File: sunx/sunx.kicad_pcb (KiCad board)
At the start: 2 copper layers, 54 x 32 mm, 11 parts, among them J1 Conn_01x05_Socket, J2 Conn_01x04_Socket, U1 HT7333-3-SOT89, con1 Conn_01x08_MountingPin

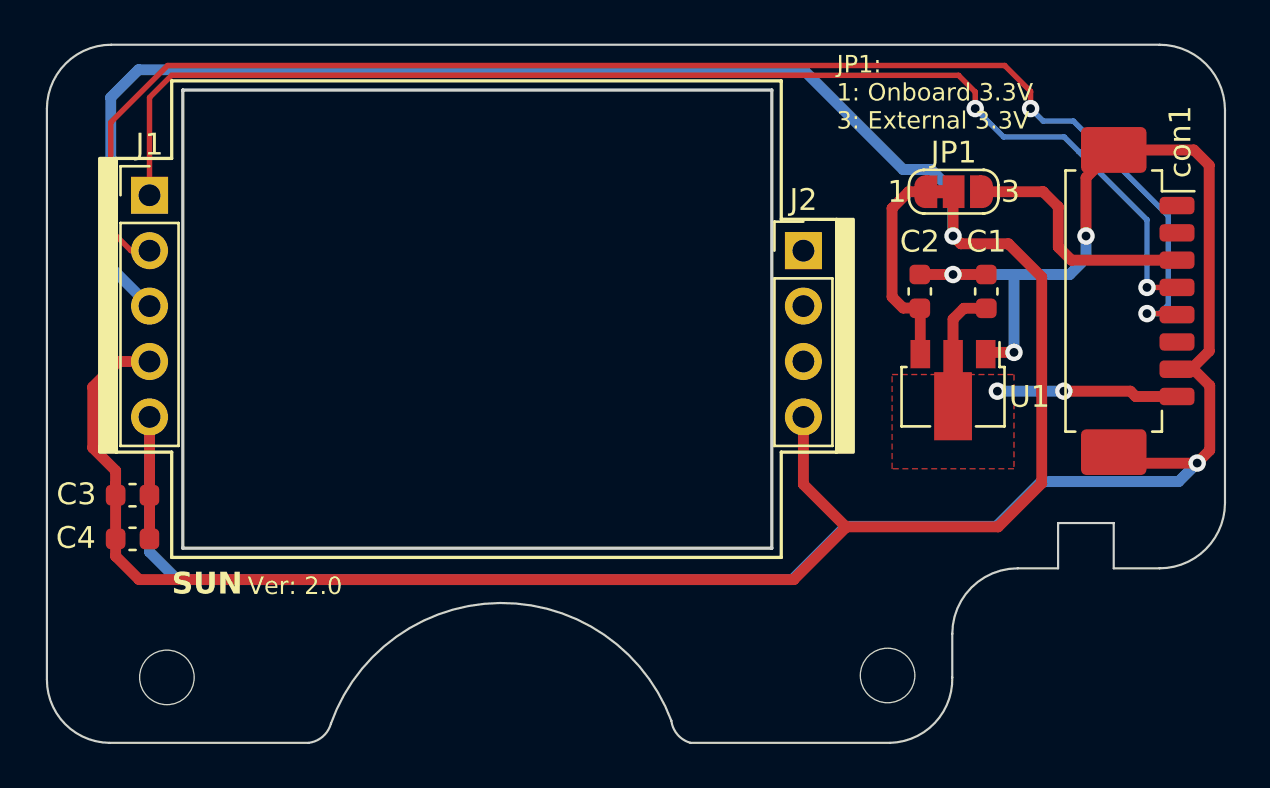
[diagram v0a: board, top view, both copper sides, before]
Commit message: WIP v2.1: AP2112K-3.3 LDO, 0R power-select links, revised placement
Carried over from Bitbucket branch V2.1 (commit 9a7380c) with the same
import-only adjustments as main. Changes on top of v2.0, per the source
commits: LDO HT7333 -> AP2112K-3.3, solder jumper JP1 replaced by 0R links
R1/R2 (R1 DNP), bulk tantalum C5 added then marked DNP ('big cap is not
needed'), silkscreen marking updated, parts moved clear of the connector.
No production set - untested and unreleased.
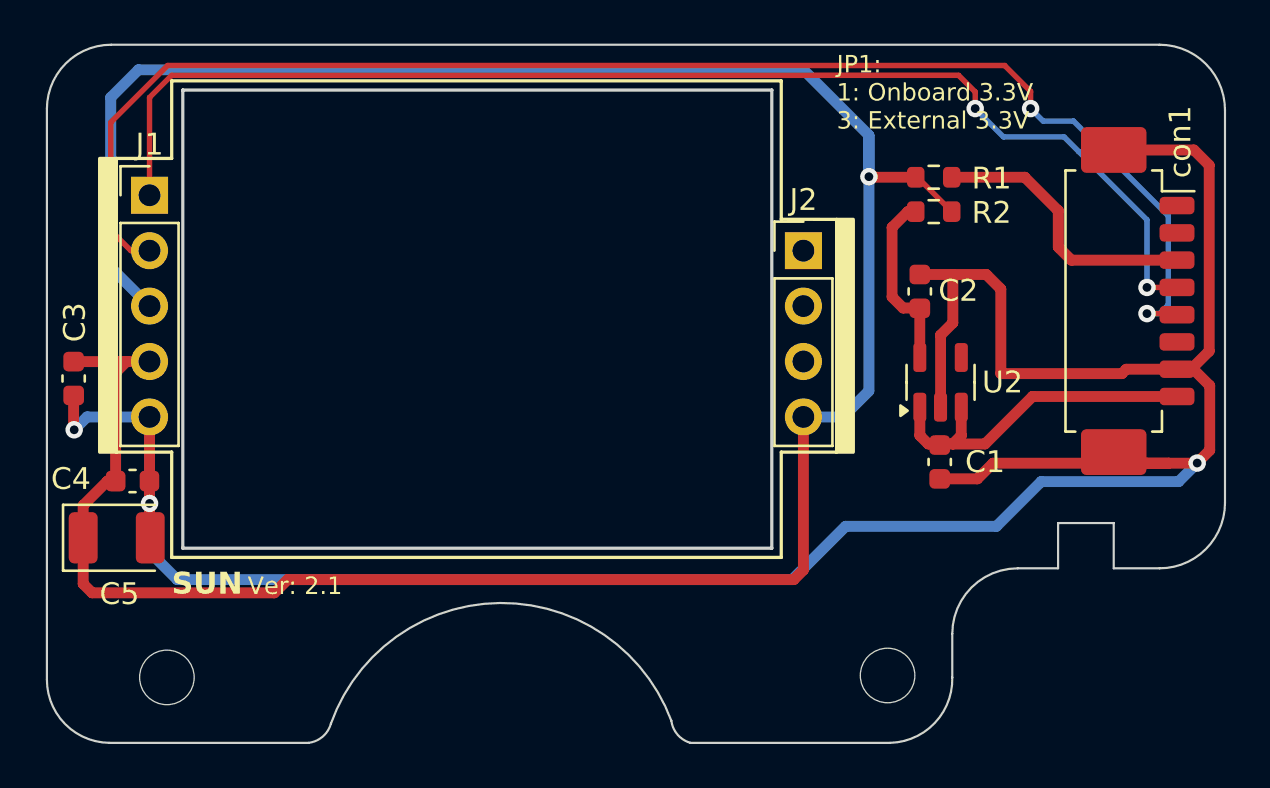
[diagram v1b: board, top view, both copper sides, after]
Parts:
- removed JP1: SolderJumper_3_Open, Jumper:SolderJumper-3_P1.3mm_Bridged12_RoundedPad1.0x1.5mm_NumberLabels
- removed U1: HT7333-3-SOT89, Package_TO_SOT_SMD:SOT-89-3
- added C5: C30242, Capacitor_Tantalum_SMD:CP_EIA-3528-21_Kemet-B, F.Cu at (43.2, 62.6)
- added R1: 0R, Resistor_SMD:R_0603_1608Metric, F.Cu at (80.7, 46.1)
- added R2: 0R, Resistor_SMD:R_0603_1608Metric, F.Cu at (80.7, 47.6)
- added U2: AP2112K-3.3, Package_TO_SOT_SMD:SOT-23-5, F.Cu at (81.0, 55.5)
- moved C1 8.10 mm to (80.9, 59.1), turned to -90 degrees
- moved C3 5.99 mm to (41.2, 55.3), turned to -90 degrees
- moved C4 2.65 mm to (43.9, 60.0)
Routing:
- net GND: track 107.9 -> 126.5 mm, vias 4 -> 3
- net /SUN_EN: track 132.1 -> 123.7 mm
- net +5V: track 11.8 -> 16.0 mm, vias 2 -> 0
- net +3.3V: track 11.3 -> 13.0 mm
- net Net-(U2-VOUT): track 9.53 -> 8.38 mm
- removed copper zone on F.Cu, net +5V
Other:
- board text added: "Ver: 2.1"
- board text removed: "Ver: 2.0"
